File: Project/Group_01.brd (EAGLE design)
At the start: 160 x 100 mm, 1 part

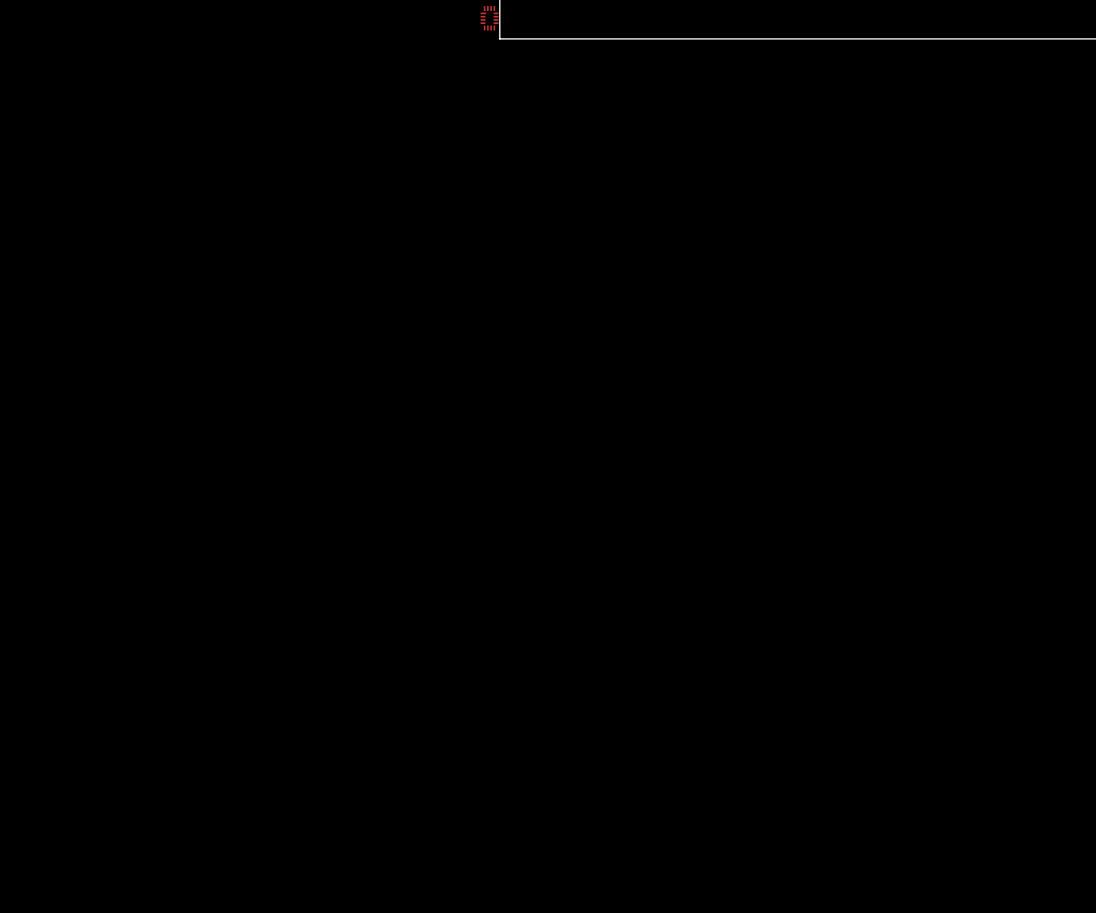
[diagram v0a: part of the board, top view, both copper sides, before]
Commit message: Added all components to schematics
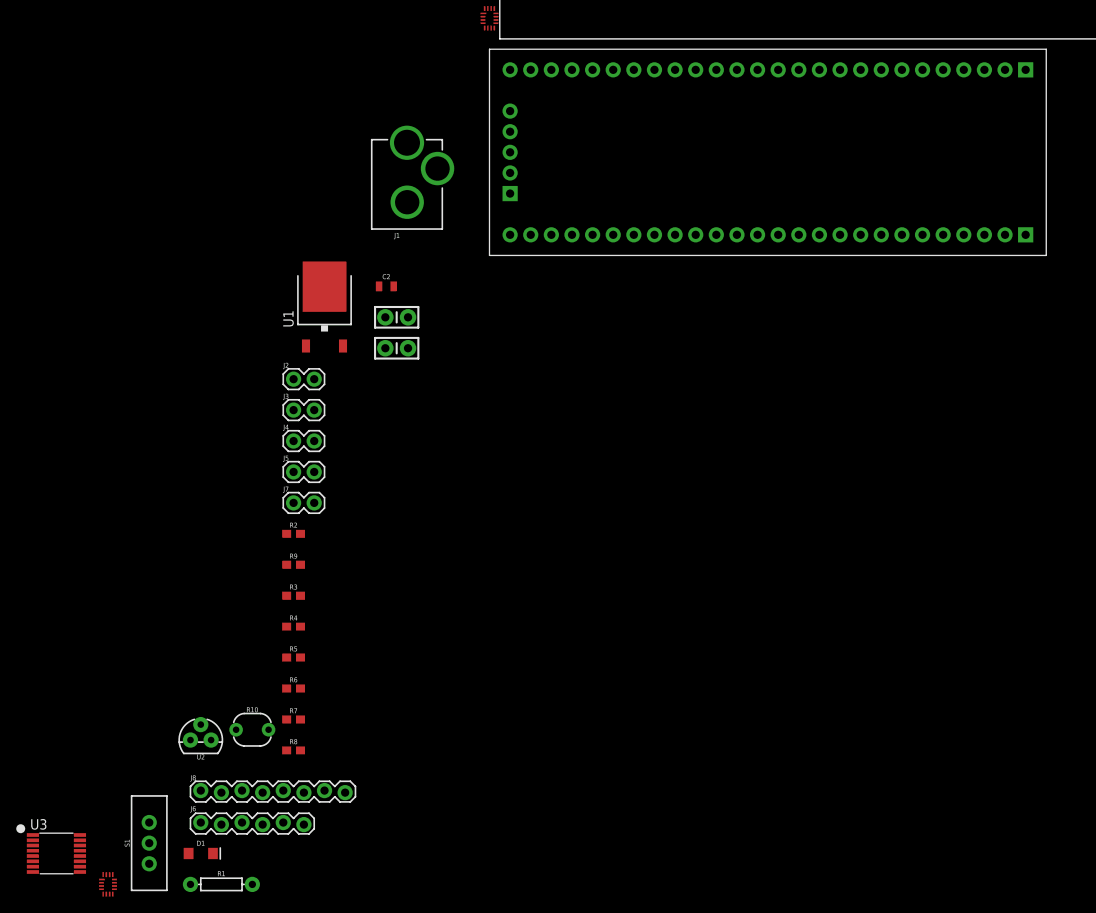
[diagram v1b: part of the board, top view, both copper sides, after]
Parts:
- added C1, C3: 0.1uF, SparkFun-Capacitors:CAP-PTH-SMALL-KIT
- added C2: 0.33µF, SparkFun-Capacitors:0805
- added D1: BLUE, SparkFun-LED:LED-1206
- added J1: POWER_JACKPTH_LOCK, SparkFun-Connectors:POWER_JACK_PTH_LOCK
- added J2, J3, J4, J5, J7: (no value), SparkFun-Connectors:1X02
- added J6: (no value), SparkFun-Connectors:1X06_LOCK
- added J8: (no value), SparkFun-Connectors:1X08_LOCK
- added R1: (no value), SparkFun-Resistors:AXIAL-0.3
- added R10: PHOTOCELLPTH, SparkFun-Sensors:PHOTOCELL
- added R2, R3, R4, R5, R6, R7, R8, R9: 4.7k, SparkFun-Resistors:0603
- added S1: (no value), SparkFun-Switches:SWITCH_SPDT_PTH_11.6X4.0MM
- added U$2: CY8CKIT-059_TARGET, CY8KIT-059:CY8CKIT-059_TARGET
- added U1: +12v, SparkFun-IC-Power:TO-252
- added U2: (no value), SparkFun-Sensors:TO-92
- added U3: TCA9546APWR, Group_01_Library:TSSOP
- added U4: TMUX1208, Group_01_Library:QFN16

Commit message: Schematics changes
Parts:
- added R11: 10k, SparkFun-Resistors:0603
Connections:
- new net 12V: C2.1, S1.1, U1.1
- new net 5V: C1.1, J7.2, R10.2, U1.2, U2.1
- new net GND: C1.2, C2.2, J1.GND, J1.GNDBREAK, J7.1, R11.1, U1.3, U2.3
- new net N$1: J1.PWR, S1.2
- new net PHOTO_OUT: R10.1, R11.2
- new net TEMP_OUT: U2.2
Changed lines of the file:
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@@
 <attribute name="VALUE" x="-57.96" y="-104.48" size="1.27" layer="27"/>
+</element>
+<element name="R11" library="SparkFun-Resistors" package="0603" value="10k" x="-57.15" y="-107.95" smashed="yes">
+<attribute name="NAME" x="-57.15" y="-107.188" size="0.6096" layer="25" font="vector" ratio="20" align="bottom-center"/>
+<attribute name="PROD_ID" value="RES-00824" x="-57.15" y="-107.95" size="1.778" layer="27" display="off"/>
+<attribute name="VALUE" x="-57.15" y="-108.712" size="0.6096" layer="27" font="vector" ratio="20" align="top-center"/>
 </element>
 </elements>
 <signals>
+<signal name="GND">
+<contactref element="J7" pad="1"/>
+<contactref element="R11" pad="1"/>
+<contactref element="U2" pad="3"/>
+<contactref element="J1" pad="GNDBREAK"/>
+<contactref element="J1" pad="GND"/>
+<contactref element="C2" pad="2"/>
+<contactref element="C1" pad="2"/>
+<contactref element="U1" pad="3"/>
+<wire x1="-35.56" y1="-86.36" x2="-58" y2="-107.95" width="0" layer="19" extent="1-1"/>
+<wire x1="-25.4" y1="-57.15" x2="-35.56" y2="-86.36" width="0" layer="19" extent="1-1"/>
+<wire x1="-11.303" y1="-34.29" x2="-25.4" y2="-57.15" width="0" layer="19" extent="1-1"/>
+<wire x1="-13.07" y1="-30.48" x2="-11.303" y2="-34.29" width="0" layer="19" extent="1-1"/>
+<wire x1="-21.59" y1="-30.52" x2="-13.07" y2="-30.48" width="0" layer="19" extent="1-1"/>
+<wire x1="-11.4046" y1="-20.113" x2="-13.07" y2="-30.48" width="0" layer="19" extent="1-1"/>
+<wire x1="-7.6684" y1="-15.97" x2="-11.4046" y2="-20.113" width="0" layer="19" extent="1-1"/>
+</signal>
+<signal name="5V">
+<contactref element="J7" pad="2"/>
+<contactref element="R10" pad="2"/>
+<contactref element="U2" pad="1"/>
+<contactref element="U1" pad="2"/>
+<contactref element="C1" pad="1"/>
+<wire x1="-28.48" y1="-85.09" x2="-38.1" y2="-86.36" width="0" layer="19" extent="1-1"/>
+<wire x1="-22.86" y1="-57.15" x2="-28.48" y2="-85.09" width="0" layer="19" extent="1-1"/>
+<wire x1="-19.31" y1="-37.82" x2="-22.86" y2="-57.15" width="0" layer="19" extent="1-1"/>
+<wire x1="-14.097" y1="-34.29" x2="-19.31" y2="-37.82" width="0" layer="19" extent="1-1"/>
+</signal>
+<signal name="PHOTO_OUT">
+<contactref element="R11" pad="2"/>
+<contactref element="R10" pad="1"/>
+<wire x1="-32.48" y1="-85.09" x2="-56.3" y2="-107.95" width="0" layer="19" extent="1-1"/>
+</signal>
+<signal name="TEMP_OUT">
+<contactref element="U2" pad="2"/>
+</signal>
+<signal name="N$1">
+<contactref element="J1" pad="PWR"/>
+<contactref element="S1" pad="2"/>
+<wire x1="-11.43" y1="-12.7922" x2="-43.18" y2="-99.06" width="0" layer="19" extent="1-1"/>
+</signal>
+<signal name="12V">
+<contactref element="S1" pad="1"/>
+<contactref element="U1" pad="1"/>
+<contactref element="C2" pad="1"/>
+<wire x1="-23.87" y1="-37.82" x2="-43.18" y2="-96.52" width="0" layer="19" extent="1-1"/>
+<wire x1="-14.87" y1="-30.48" x2="-23.87" y2="-37.82" width="0" layer="19" extent="1-1"/>
+</signal>
 </signals>
 <mfgpreviewcolors>

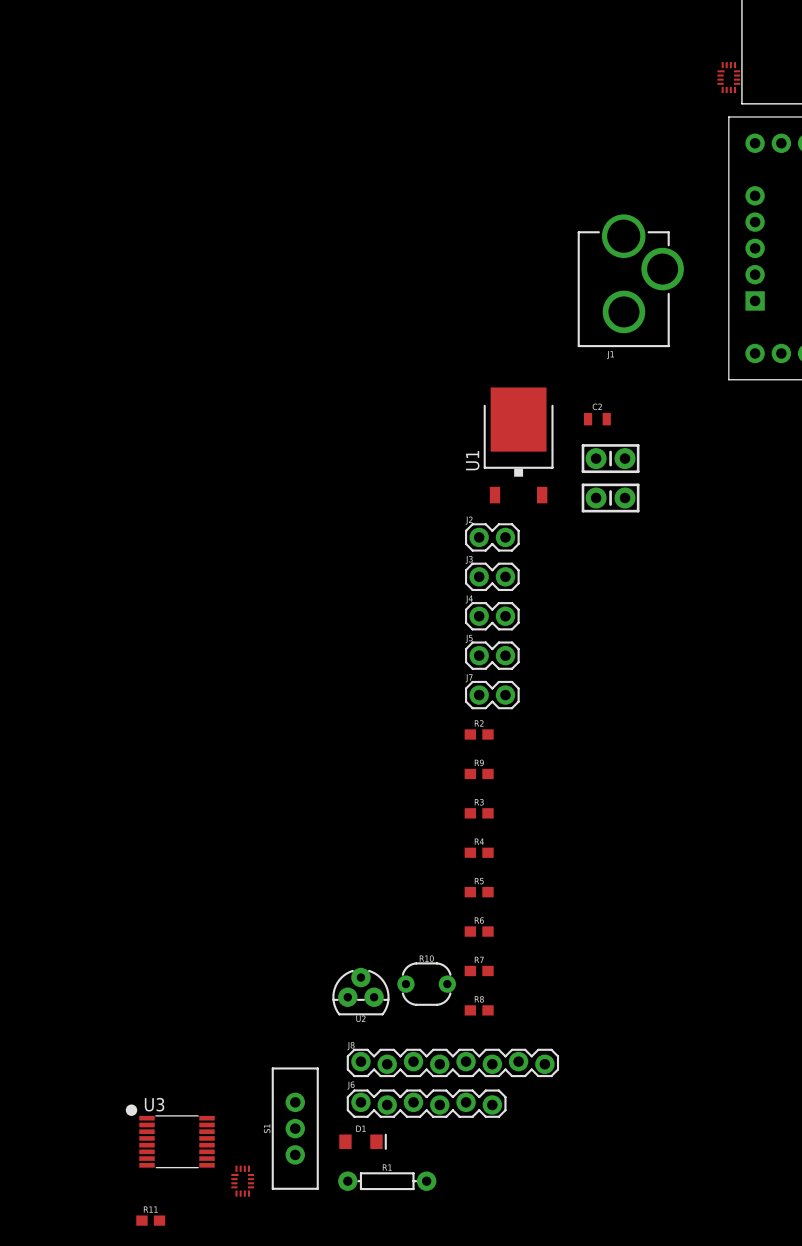
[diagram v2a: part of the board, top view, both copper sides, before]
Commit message: Schematic update
Microcontroller, TCA and connectors all connected
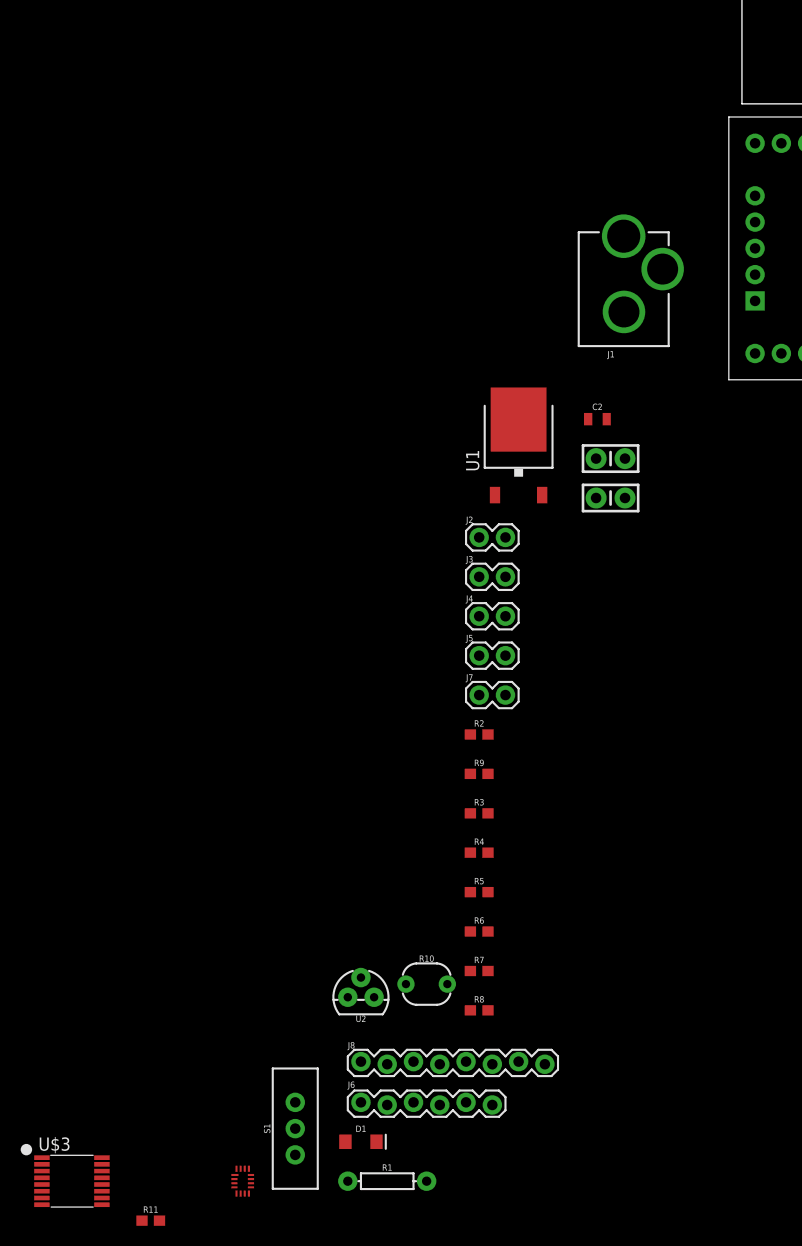
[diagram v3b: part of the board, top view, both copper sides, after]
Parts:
- removed U$1: TMUX1208, Group_01_Library:QFN16
- removed U3: TCA9546APWR, Group_01_Library:TSSOP
- added U$3: TCA9546A, Group_01_Library:TSSOP16
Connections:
- new net I2C_A0: U$2.6, U$3.1
- new net I2C_A1: U$2.7, U$3.2
- new net I2C_A2: U$2.8, U$3.13
- new net I2C_SCL: U$2.16, U$3.14
- new net I2C_SCL_0: J2.2, R2.1, U$3.5
- new net I2C_SCL_1: J3.2, R8.1, U$3.7
- new net I2C_SCL_2: J4.2, R4.1, U$3.10
- new net I2C_SCL_3: J5.2, R6.1, U$3.12
- new net I2C_SDA: U$2.15, U$3.15
- new net I2C_SDA_0: J2.1, R3.1, U$3.4
- new net I2C_SDA_1: J3.1, R9.1, U$3.6
- new net I2C_SDA_2: J4.1, R5.1, U$3.9
- new net I2C_SDA_3: J5.1, R7.1, U$3.11
- new net MUX_A0/2.3C: U$2.24
- new net MUX_A1/2.3C: U$2.23
- new net MUX_A2/2.3C: U$2.22
- new net MUX_OUT/2.5C: U$2.21
- new net N$2: J6.1, U$2.32
- new net N$3: J6.2, U$2.33
- new net N$4: J6.3, U$2.34
- new net N$5: J6.4, U$2.35
- new net N$6: J6.5, U$2.36
- new net N$7: J6.6, U$2.37
- new net N$8: D1.A, U$2.51
- new net N$9: D1.C, R1.P$2
- net 5V: now also R2.2, R3.2, R4.2, R5.2, R6.2, R7.2, R8.2, R9.2, U$2.26, U$2.27, U$3.16
- net GND: now also R1.P$1, U$2.25, U$2.28, U$3.3, U$3.8
- net PHOTO_OUT: now also U$2.44
- net TEMP_OUT: now also U$2.43

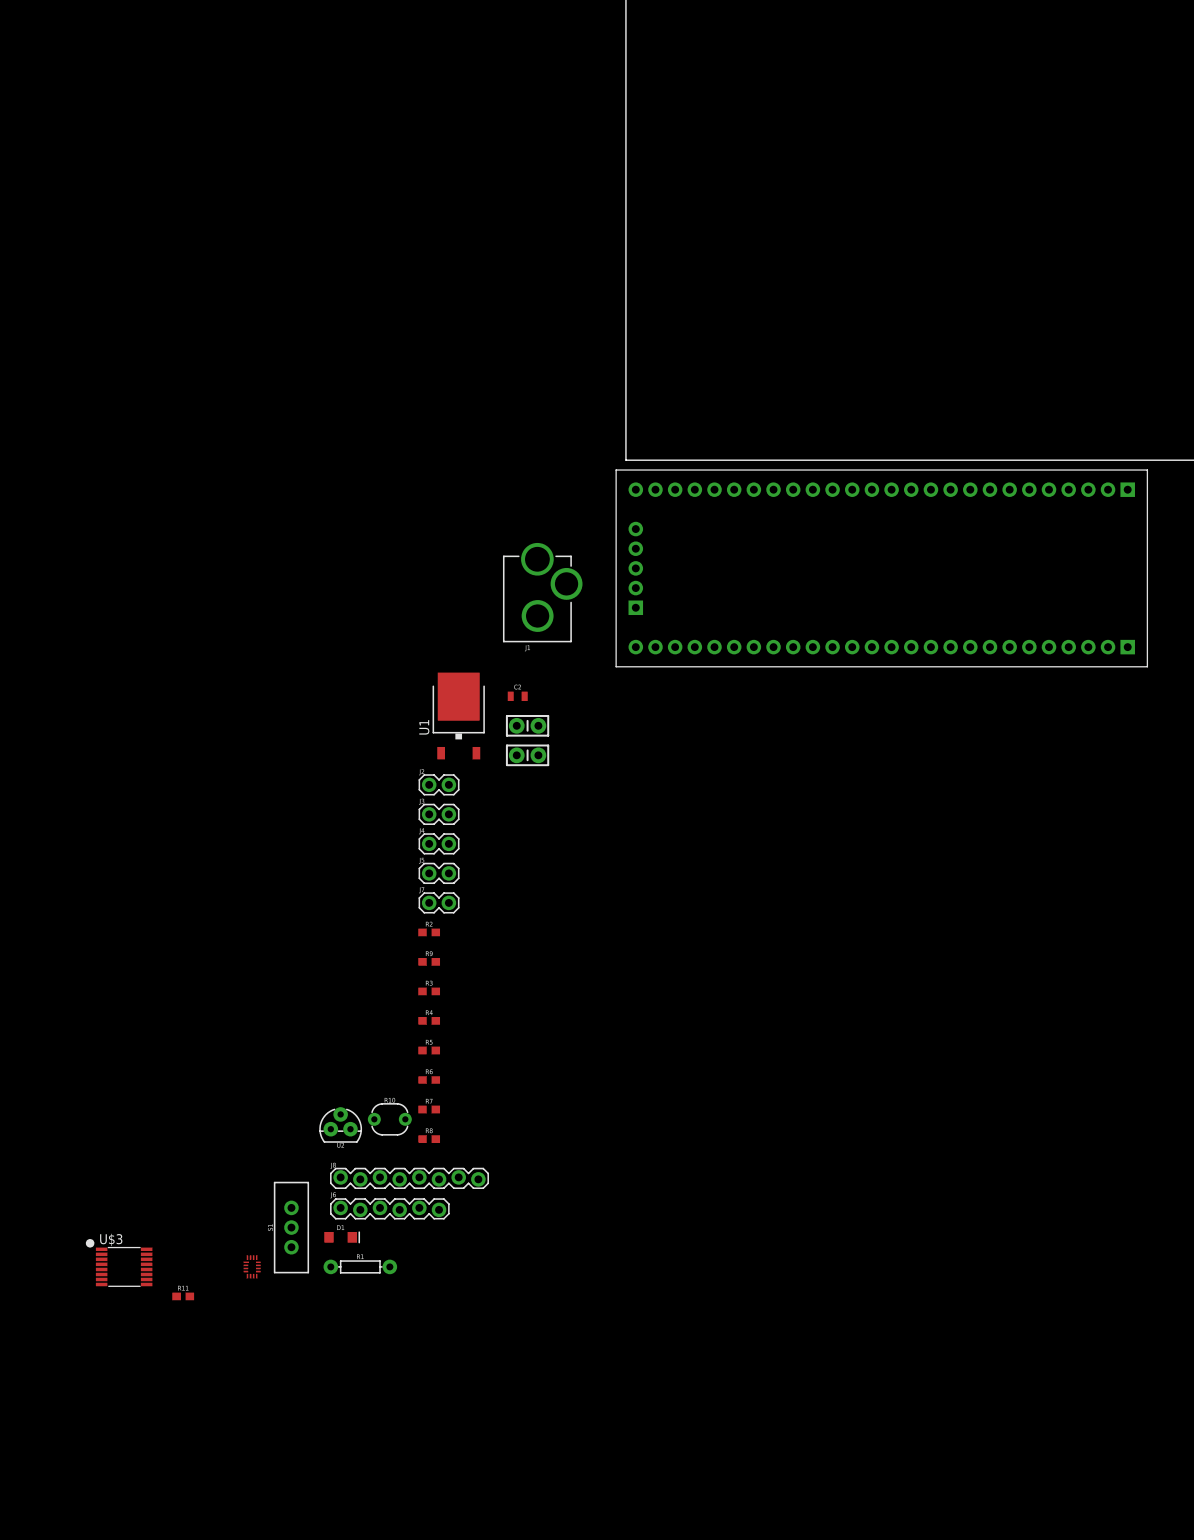
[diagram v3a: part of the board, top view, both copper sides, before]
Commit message: Changed QFN16 and finished schematics
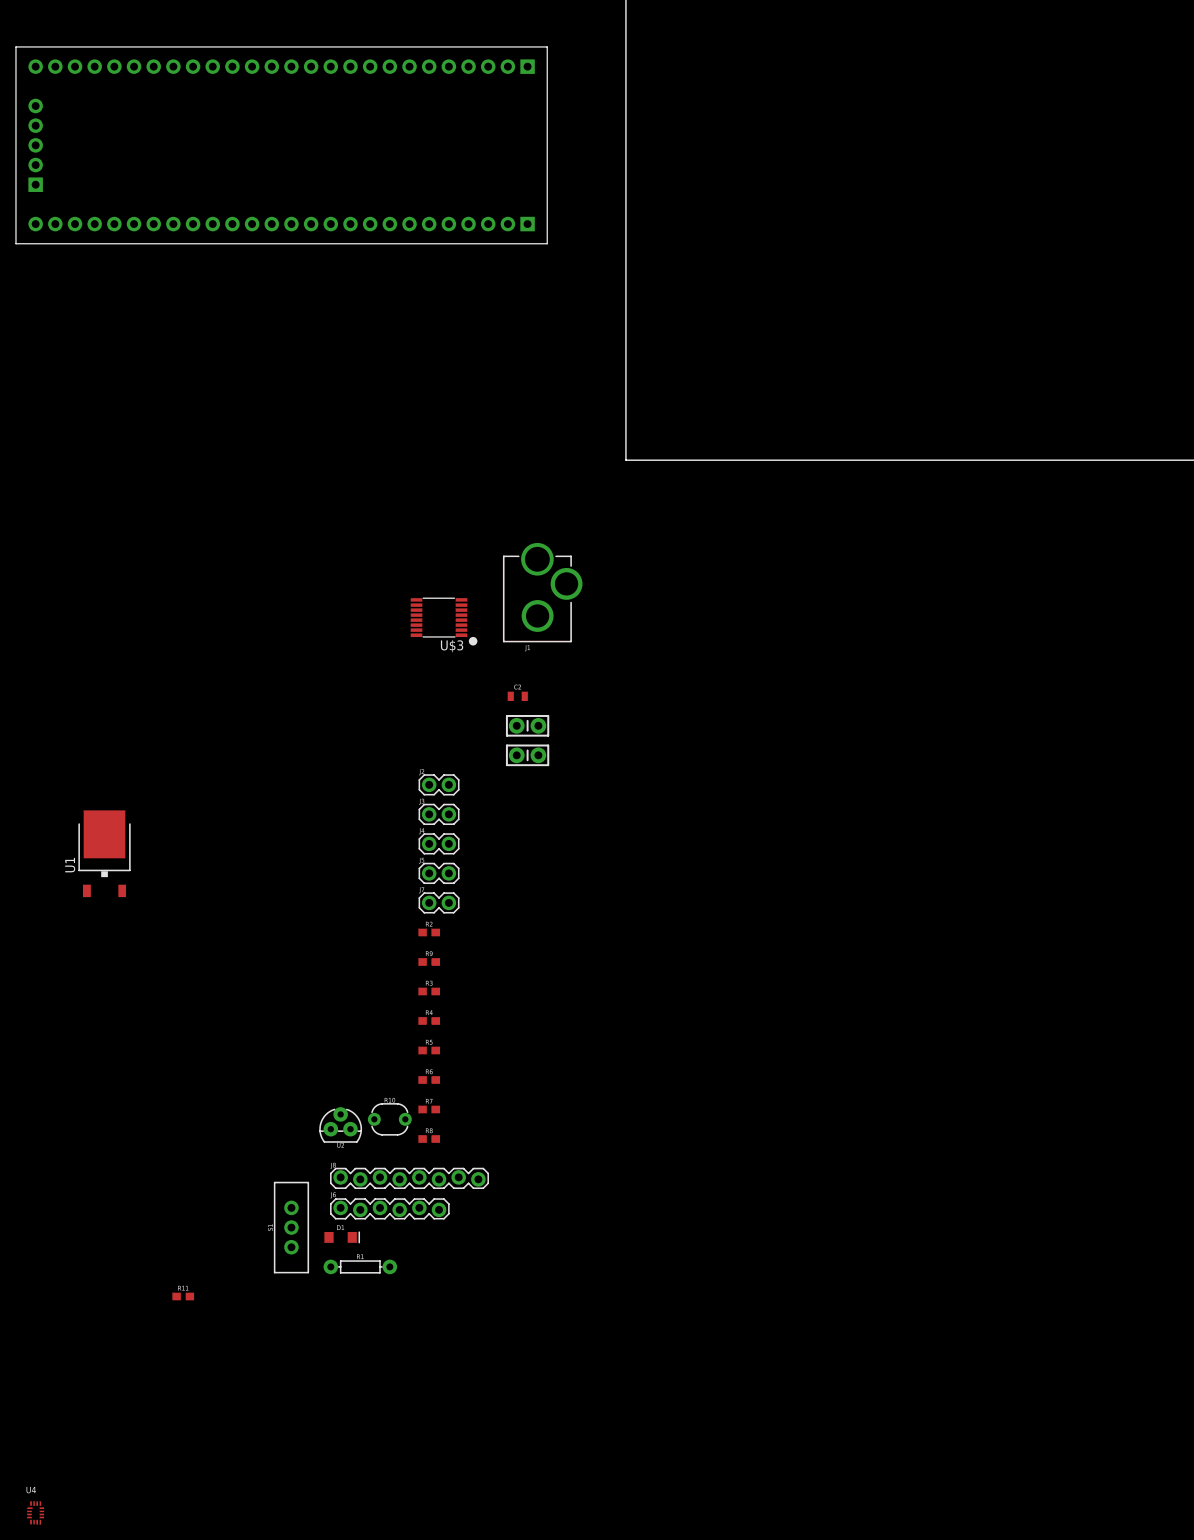
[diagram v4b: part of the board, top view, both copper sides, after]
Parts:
- moved U$2 94.8 mm to (-43.2, 41.9)
- moved U$3 93.2 mm to (-24.1, -20.3), turned to 180 degrees
- moved U1 49.1 mm to (-67.3, -50.8)
- moved U4 42.3 mm to (-76.2, -135.9)
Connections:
- new net MUX_A0/1.3C: U4.A0
- new net MUX_A1/1.4C: U4.A1
- new net MUX_A2/1.4C: U4.A2
- new net MUX_OUT/1.4C: U4.D
- new net N$10: J8.8, U4.S1
- new net N$11: J8.7, U4.S2
- new net N$12: J8.6, U4.S3
- new net N$13: J8.5, U4.S4
- new net N$14: J8.4, U4.S5
- new net N$15: J8.3, U4.S6
- new net N$16: J8.2, U4.S7
- new net N$17: J8.1, U4.S8
- net 5V: now also C3.1, U4.EN, U4.VDD
- net GND: now also C3.2, U4.GND

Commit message: Added comments on schematic, board layout, dru file
The board still needs to be routed
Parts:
- moved U4 189.0 mm to (46.6, 7.75)
- moved D1 181.6 mm to (63.2, 51.2), turned to 180 degrees
- moved R1 178.7 mm to (54.2, 51.1)
- moved R11 162.4 mm to (57.5, 7.12), turned to 270 degrees
- moved U2 160.5 mm to (44.8, 51.8), turned to 180 degrees
- moved J6 157.7 mm to (16.5, 51.9)
- moved R7 135.1 mm to (60.3, 20.6), turned to 90 degrees
- moved R5 131.6 mm to (63.9, 20.6), turned to 90 degrees
- moved R6 131.0 mm to (58.5, 20.6), turned to 90 degrees
- moved J8 130.5 mm to (53.1, 1.89), turned to 180 degrees
- moved R8 129.9 mm to (63.5, 7.10), turned to 270 degrees
- moved R4 127.7 mm to (62.1, 20.5), turned to 90 degrees
- moved J5 118.6 mm to (69.2, 18.1), turned to 90 degrees
- moved S1 117.8 mm to (16.2, 2.68), turned to 270 degrees
- moved U1 116.0 mm to (27.5, 16.0), turned to 270 degrees
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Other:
- board size 160 x 100 mm -> 71.1 x 54.3 mm
